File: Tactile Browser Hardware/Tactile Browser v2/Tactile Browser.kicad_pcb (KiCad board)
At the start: 4 copper layers, 74.2 x 113.2 mm, 132 parts, among them SW1 SW_Push, SW10 SW_Push, SW11 SW_Push, SW12 SW_Push, SW13 SW_Push, SW14 SW_Push, SW15 SW_Push, SW16 SW_Push, SW17 SW_Push, SW18 SW_Push, SW2 SW_Push, SW3 SW_Push, SW4 SW_Push, SW5 SW_Push, SW6 SW_Push, SW7 SW_Push, SW8 SW_Push, SW9 SW_Push

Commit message: PCB almost done!
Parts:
- removed 100uF1, 100uF2: C, Capacitor_SMD:C_0805_2012Metric
- uF10: renamed from 100uF10; moved to B.Cu
- uF9: renamed from 100uF9; moved to B.Cu
- moved uF8 127.6 mm to (51.0, 110.8), turned to 90 degrees
- moved uF18 113.8 mm to (87.0, 129.0), turned to 90 degrees
- moved uF17 112.7 mm to (87.0, 124.7), turned to 90 degrees
- moved uF7 107.6 mm to (56.8, 110.8), turned to -90 degrees
- moved uF15 100.8 mm to (88.2, 105.0), turned to 90 degrees
- moved uF6 96.7 mm to (50.2, 75.8), turned to 90 degrees
- moved uF4 95.4 mm to (50.5, 66.8), turned to 90 degrees
- moved uF16 92.6 mm to (88.2, 97.5), turned to -90 degrees
- moved uF5 91.5 mm to (57.2, 75.8), turned to -90 degrees
- moved 5V 83.3 mm to (64.0, 120.7), turned to -90 degrees
- moved uF3 77.2 mm to (56.8, 66.5), turned to 90 degrees
- moved uF13 65.0 mm to (90.8, 76.2), turned to 90 degrees
- moved uF11 63.0 mm to (91.0, 67.0), turned to -90 degrees
- moved uF9 57.5 mm to (88.5, 41.0), turned to -90 degrees
- moved uF14 57.0 mm to (98.2, 76.0), turned to 90 degrees
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- renumbered 100nF1 to uF1, 100uF11 to uF11, 100uF12 to uF12, 100uF13 to uF13, 100uF14 to uF14, 100uF15 to uF15, 100uF16 to uF16, 100uF17 to uF17, 100uF18 to uF18, 100nF2 to uF2, 100uF3 to uF3, 100uF4 to uF4, 100uF5 to uF5, 100uF6 to uF6, 100uF7 to uF7, 100uF8 to uF8
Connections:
- DS10 pad 2: S6_out1 -> S5_out2
- DS11 pad 2: S5_out2 -> S6_out1
- DS12 pad 2: S5_out1 -> S6_out2
- DS9 pad 2: S6_out2 -> S5_out1
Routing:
- net 12V: track 46.8 -> 195.2 mm, vias 4 -> 6
- net Col1: track 9.19 -> 122.4 mm, vias 0 -> 2
- net Row1: track 22.3 -> 130.5 mm, vias 0 -> 1
- net Row2: track 1.54 -> 108.7 mm, vias 0 -> 1
- net Col2: track 0.00 -> 104.1 mm, vias 0 -> 5
- net Col3: track 0.00 -> 100.7 mm
- net Row3: track 0.00 -> 99.4 mm, vias 0 -> 3
- net Row5: track 0.00 -> 93.7 mm, vias 0 -> 5
- net Row4: track 0.00 -> 92.0 mm, vias 0 -> 1
- net DATA: track 0.00 -> 91.6 mm, vias 0 -> 1
- net Row6: track 0.00 -> 81.5 mm, vias 0 -> 3
- net CLOCK: track 0.00 -> 49.6 mm, vias 0 -> 2
- net LATCH: track 0.00 -> 47.2 mm, vias 0 -> 2
- net GND: track 22.1 -> 67.2 mm
- net 5V: track 13.5 -> 40.5 mm, vias 2 -> 7
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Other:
- board size 74.2 x 113.2 mm -> 74.5 x 110.2 mm

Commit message: more pcb work
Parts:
- turned DS18 to -90 degrees
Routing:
- net STBY: track 27.5 -> 112.2 mm, vias 2 -> 5
- net CLOCK: track 49.6 -> 106.7 mm, vias 2 -> 5
- net LATCH: track 47.2 -> 102.9 mm, vias 2 -> 3
- net PWM: track 23.0 -> 75.0 mm, vias 2 -> 5
- net GND: track 67.2 -> 109.3 mm, vias 2 -> 15
- net Overflow1: track 0.00 -> 41.9 mm, vias 0 -> 2
- net 12V: track 195.2 -> 231.6 mm, vias 6 -> 15
- net 5V: track 40.5 -> 56.3 mm
- net S9_out1: track 0.00 -> 15.4 mm, vias 0 -> 1
- net S9_out2: track 0.00 -> 14.6 mm
- net (no net): track 4.91 -> 0.00 mm
- net S5_in1: track 8.54 -> 9.68 mm

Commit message: almost done with pcb!
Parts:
- moved uF11 7.00 mm to (98.0, 67.0)
- moved uF12 6.75 mm to (91.0, 67.0)
- moved uF9 4.00 mm to (88.5, 37.0), turned to 90 degrees
- moved uF10 3.80 mm to (88.5, 40.8), turned to 90 degrees
- moved uF17 0.85 mm to (87.8, 124.3)
- moved uF18 0.85 mm to (87.8, 128.6)
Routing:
- net PWM: track 75.0 -> 369.4 mm, vias 5 -> 16
- net 12V: track 231.6 -> 410.2 mm, vias 15 -> 67
- net GND: track 109.3 -> 257.5 mm, vias 15 -> 57
- net STBY: track 112.2 -> 214.1 mm, vias 5 -> 12
- net 5V: track 56.3 -> 148.4 mm, vias 7 -> 16
- net Overflow2: track 0.00 -> 85.5 mm, vias 0 -> 2
- net SDA: track 0.00 -> 62.6 mm
- net Overflow3: track 0.00 -> 60.0 mm, vias 0 -> 2
- net SCL: track 0.00 -> 53.3 mm
- net S10_out1: track 0.00 -> 46.8 mm
- net S12_out1: track 0.00 -> 43.8 mm
- net S18_out1: track 0.00 -> 41.2 mm
- net S16_out1: track 0.00 -> 39.3 mm
- net S14_out2: track 0.00 -> 37.0 mm, vias 0 -> 1
- net S18_out2: track 0.00 -> 36.4 mm, vias 0 -> 1
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
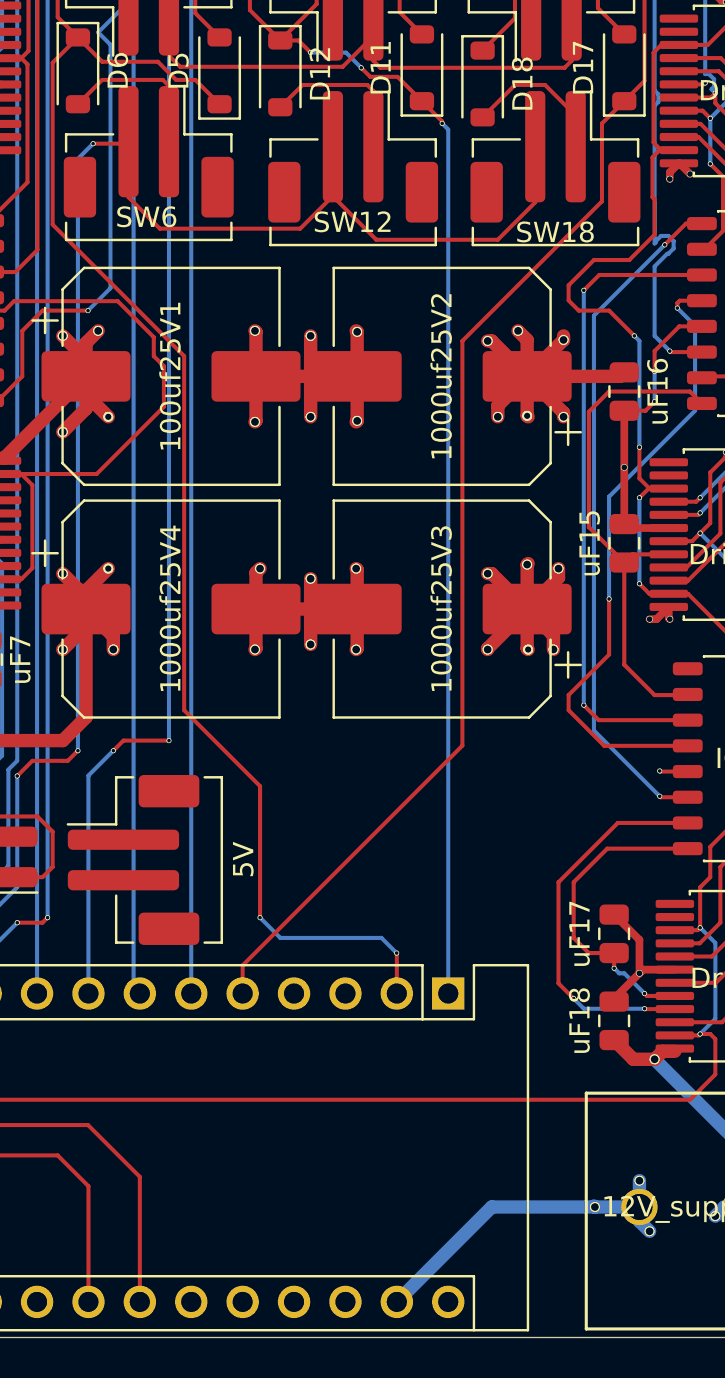
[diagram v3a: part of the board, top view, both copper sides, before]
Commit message: ground +12V planes
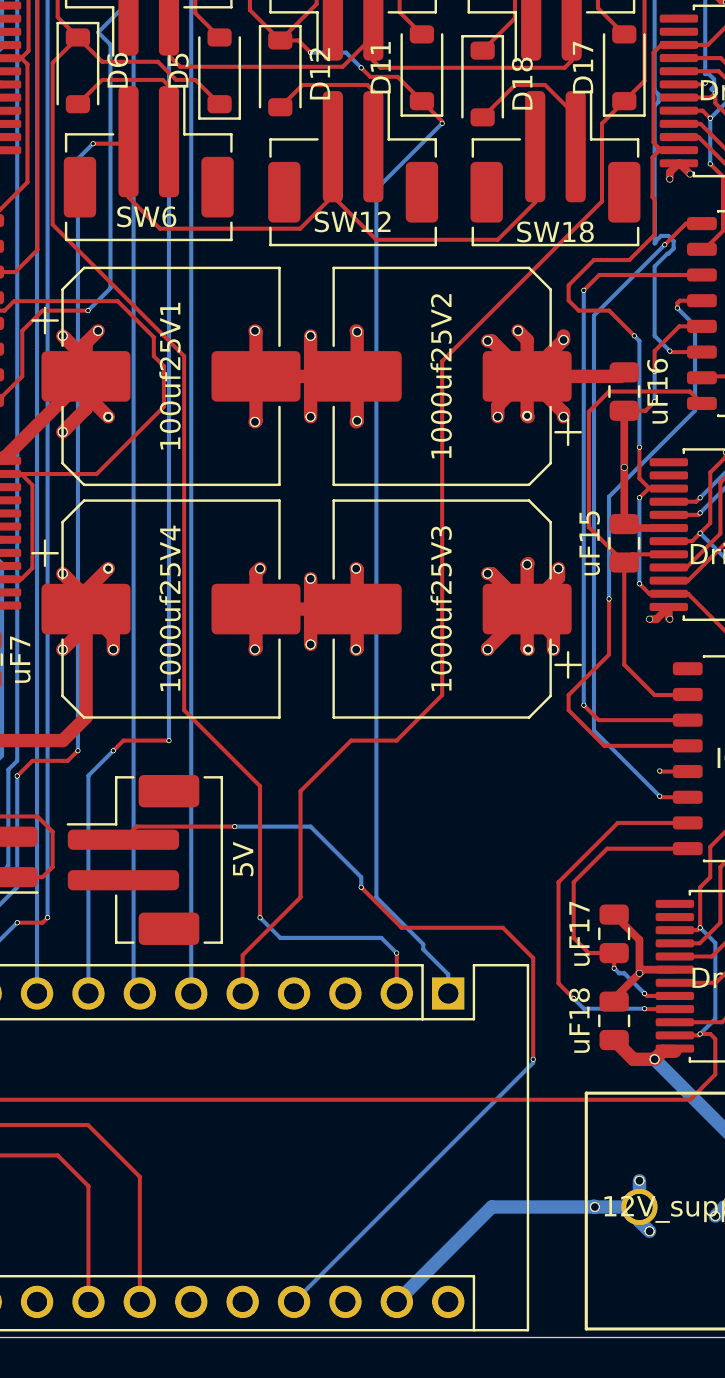
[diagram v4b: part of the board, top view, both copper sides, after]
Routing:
- net 5V: track 148.4 -> 193.8 mm, vias 16 -> 19
- net Col2: track 104.1 -> 106.8 mm
- net Col3: track 100.7 -> 102.0 mm
- removed copper zone on In2.Cu, net 12V
- removed copper zone on In1.Cu, net GND
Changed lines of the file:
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@@
 		(net 8)
 	)
+	(gr_poly
+		(pts
+			(xy 37 34) (xy 111.5 34) (xy 111.5 144.25) (xy 37 144.25)
+		)
+		(stroke
+			(width 0.2)
+			(type solid)
+		)
+		(fill yes)
+		(layer "In1.Cu")
+	)
 	(gr_rect
 		(start 37 34)
@@
 	)
 	(segment
+		(start 82.25 124)
+		(end 83.75 125.5)
+		(width 0.2032)
+		(layer "F.Cu")
+		(net 1)
+	)
+	(segment
 		(start 56.8625 89.055)
 		(end 58.7558 87.1617)
@@
 	)
 	(segment
+		(start 77.25 124)
+		(end 82.25 124)
+		(width 0.2032)
+		(layer "F.Cu")
+		(net 1)
+	)
+	(segment
 		(start 91.497401 97.5)
 		(end 87.5 97.5)
@@
 	)
 	(segment
+		(start 83.75 125.5)
+		(end 83.75 130.5)
+		(width 0.2032)
+		(layer "F.Cu")
+		(net 1)
+	)
+	(segment
 		(start 90.950001 61.6951)
 		(end 92.3049 61.6951)
@@
 	)
 	(segment
+		(start 64.15 119)
+		(end 69 119)
+		(width 0.2032)
+		(layer "F.Cu")
+		(net 1)
+	)
+	(segment
 		(start 89.25 38.870098)
 		(end 89.25 38.75)
@@
 	)
 	(segment
+		(start 63.5 119.65)
+		(end 64.15 119)
+		(width 0.2032)
+		(layer "F.Cu")
+		(net 1)
+	)
+	(segment
 		(start 91.95 77.2)
 		(end 90.75 77.2)
@@
 	)
 	(segment
+		(start 75.25 122)
+		(end 77.25 124)
+		(width 0.2032)
+		(layer "F.Cu")
+		(net 1)
+	)
+	(segment
 		(start 98 66.05)
 		(end 96.8 66.05)
@@
 	)
 	(via
+		(at 69 119)
+		(size 0.254)
+		(drill 0.1778)
+		(layers "F.Cu" "B.Cu")
+		(net 1)
+	)
+	(via
 		(at 92.5 86.25)
 		(size 0.254)
@@
 	)
 	(via
+		(at 83.75 130.5)
+		(size 0.254)
+		(drill 0.1778)
+		(layers "F.Cu" "B.Cu")
+		(net 1)
+	)
+	(via
 		(at 55.75 96.75)
 		(size 0.254)
@@
 	)
 	(via
+		(at 75.25 122)
+		(size 0.254)
+		(drill 0.1778)
+		(layers "F.Cu" "B.Cu")
+		(net 1)
+	)
+	(via
 		(at 90.5 44.75)
 		(size 0.254)
@@
 	)
 	(segment
+		(start 83.75 130.67)
+		(end 71.93 142.49)
+		(width 0.2032)
+		(layer "B.Cu")
+		(net 1)
+	)
+	(segment
 		(start 55.5 43.75)
 		(end 55.75 44)
@@
 	)
 	(segment
+		(start 75.25 122)
+		(end 75.25 121.5)
+		(width 0.2032)
+		(layer "B.Cu")
+		(net 1)
+	)
+	(segment
 		(start 93.5 83)
 		(end 93.5 78.5)
@@
 	)
 	(segment
+		(start 83.75 130.5)
+		(end 83.75 130.67)
+		(width 0.2032)
+		(layer "B.Cu")
+		(net 1)
+	)
+	(segment
 		(start 92.5 84)
 		(end 92.5 86.25)
@@
 	)
 	(segment
+		(start 75.25 121.5)
+		(end 72.75 119)
+		(width 0.2032)
+		(layer "B.Cu")
+		(net 1)
+	)
+	(segment
 		(start 59.25 38)
 		(end 58.75 37.5)
@@
 	)
 	(segment
+		(start 72.75 119)
+		(end 69 119)
+		(width 0.2032)
+		(layer "B.Cu")
+		(net 1)
+	)
+	(segment
 		(start 90.5 44.75)
 		(end 90.75 44.5)
@@
 	)
 	(segment
-		(start 87.149 84.251)
-		(end 87.149 88.101)
-		(width 0.2)
-		(layer "F.Cu")
-		(net 24)
-	)
-	(segment
 		(start 87.049 64.599)
 		(end 88.25 65.8)
@@
 	)
 	(segment
-		(start 81.25 44.5)
-		(end 82.451 45.701)
+		(start 69.39 127.25)
+		(end 69.39 125.36)
 		(width 0.2)
 		(layer "F.Cu")
@@
 	)
 	(segment
-		(start 80.25 115)
-		(end 69.39 125.86)
+		(start 72.25 117.25)
+		(end 74.75 114.75)
 		(width 0.2)
 		(layer "F.Cu")
@@
 	)
 	(segment
-		(start 82.849 75.66484)
-		(end 85.01384 73.5)
+		(start 81.25 44.5)
+		(end 82.451 45.701)
 		(width 0.2)
 		(layer "F.Cu")
@@
 	)
 	(segment
-		(start 87.301 45.701)
-		(end 88.25 46.65)
+		(start 82.849 75.66484)
+		(end 85.01384 73.5)
 		(width 0.2)
 		(layer "F.Cu")
@@
 	)
 	(segment
-		(start 88.25 83.15)
-		(end 87.149 84.251)
+		(start 87.301 45.701)
+		(end 88.25 46.65)
 		(width 0.2)
 		(layer "F.Cu")
@@
 	)
 	(segment
-		(start 89.251 74)
-		(end 89.251 66.801)
+		(start 87.149 88.101)
+		(end 79.25 96)
 		(width 0.2)
 		(layer "F.Cu")
@@
 	)
 	(segment
-		(start 69.39 125.86)
-		(end 69.39 127.25)
+		(start 77 114.75)
+		(end 79.25 112.5)
+		(width 0.2)
+		(layer "F.Cu")
+		(net 24)
+	)
+	(segment
+		(start 89.251 74)
+		(end 89.251 66.801)
 		(width 0.2)
 		(layer "F.Cu")
@@
 	)
 	(segment
+		(start 74.75 114.75)
+		(end 77 114.75)
+		(width 0.2)
+		(layer "F.Cu")
+		(net 24)
+	)
+	(segment
+		(start 87.149 84.251)
+		(end 87.149 88.101)
+		(width 0.2)
+		(layer "F.Cu")
+		(net 24)
+	)
+	(segment
+		(start 79.25 96)
+		(end 79.25 112.5)
+		(width 0.2)
+		(layer "F.Cu")
+		(net 24)
+	)
+	(segment
+		(start 69.39 125.36)
+		(end 72.25 122.5)
+		(width 0.2)
+		(layer "F.Cu")
+		(net 24)
+	)
+	(segment
 		(start 82.451 45.701)
 		(end 87.301 45.701)
@@
 	)
 	(segment
-		(start 87.149 88.101)
-		(end 80.25 95)
+		(start 88.25 83.15)
+		(end 87.149 84.251)
 		(width 0.2)
 		(layer "F.Cu")
@@
 	)
 	(segment
-		(start 80.25 95)
-		(end 80.25 115)
+		(start 81.25 62.5)
+		(end 83.349 64.599)
 		(width 0.2)
 		(layer "F.Cu")
@@
 	)
 	(segment
-		(start 81.25 62.5)
-		(end 83.349 64.599)
+		(start 72.25 122.5)
+		(end 72.25 117.25)
 		(width 0.2)
 		(layer "F.Cu")
@@
 	)
 	(segment
-		(start 74.5 80.75)
-		(end 75.25 81.5)
+		(start 79.25 84.25)
+		(end 76 87.5)
+		(width 0.2)
+		(layer "B.Cu")
+		(net 27)
+	)
+	(segment
+		(start 76 122.5)
+		(end 78.317787 124.817787)
 		(width 0.2)
 		(layer "B.Cu")
@@
 	)
 	(segment
-		(start 79.55 127.25)
-		(end 79.55 84.55)
+		(start 78.317787 125.067787)
+		(end 79.55 126.3)
 		(width 0.2)
 		(layer "B.Cu")
@@
 	)
 	(segment
-		(start 79.55 84.55)
-		(end 79.25 84.25)
+		(start 79.55 126.3)
+		(end 79.55 127.25)
+		(width 0.2)
+		(layer "B.Cu")
+		(net 27)
+	)
+	(segment
+		(start 76 87.5)
+		(end 76 122.5)
+		(width 0.2)
+		(layer "B.Cu")
+		(net 27)
+	)
+	(segment
+		(start 78.317787 124.817787)
+		(end 78.317787 125.067787)
+		(width 0.2)
+		(layer "B.Cu")
+		(net 27)
+	)
+	(segment
+		(start 74.5 80.75)
+		(end 75.25 81.5)
 		(width 0.2)
 		(layer "B.Cu")
@@
 		(net 125)
 	)
-	(zone
-		(net 2)
-		(net_name "GND")
-		(layer "In1.Cu")
-		(hatch edge 0.5)
-		(connect_pads
-			(clearance 0.5)
-		)
-		(min_thickness 0.25)
-		(filled_areas_thickness no)
-		(fill yes
-			(thermal_gap 0.5)
-			(thermal_bridge_width 0.5)
-		)
-		(polygon
-			(pts
-				(xy 37 34) (xy 129 34) (xy 129 149) (xy 37 149)
-			)
-		)
-	)
-	(zone
-		(net 3)
-		(net_name "12V")
-		(layer "In2.Cu")
-		(hatch edge 0.5)
-		(priority 1)
-		(connect_pads
-			(clearance 0.5)
-		)
-		(min_thickness 0.25)
-		(filled_areas_thickness no)
-		(fill yes
-			(thermal_gap 0.5)
-			(thermal_bridge_width 0.5)
-		)
-		(polygon
-			(pts
-				(xy 37 34) (xy 129 34) (xy 129 149) (xy 37 149)
-			)
-		)
-	)
 	(embedded_fonts no)

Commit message: DRC
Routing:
- net LATCH: track 133.9 -> 263.1 mm, vias 5 -> 8
- net 5V: track 193.8 -> 299.5 mm, vias 19 -> 23
- net CLOCK: track 140.1 -> 189.3 mm, vias 7 -> 8
- net STBY: track 214.1 -> 257.9 mm, vias 12 -> 13
- net Col3: track 102.0 -> 122.6 mm, vias 0 -> 2
- net Col2: track 106.8 -> 126.1 mm, vias 5 -> 7
- net S17_out1: track 14.9 -> 18.3 mm
- net 12V: track 410.2 -> 412.3 mm, vias 67 -> 69
- net S4_in2: track 13.7 -> 14.7 mm
- net Overflow3: track 60.0 -> 59.0 mm
- net S4_in1: track 14.5 -> 15.5 mm
- net S12_in1: track 17.6 -> 18.4 mm
- net GND: track 257.5 -> 256.8 mm, vias 57 -> 58
- net PWM: track 369.4 -> 368.8 mm, vias 16 -> 17
- net S5_in1: track 9.68 -> 10.2 mm
- added copper zone on In2.Cu, net 12V
- added copper zone on In1.Cu, net GND

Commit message: ran drc, finished routing
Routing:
- net CLOCK: track 189.3 -> 259.9 mm, vias 8 -> 9
- net 5V: track 299.5 -> 335.8 mm, vias 23 -> 24
- net S17_out2: track 15.8 -> 19.4 mm
- net S15_out2: track 13.6 -> 17.1 mm
- net S15_out1: track 15.2 -> 18.6 mm
- net GND: track 256.8 -> 259.2 mm, vias 58 -> 60
- net PWM: track 368.8 -> 369.6 mm

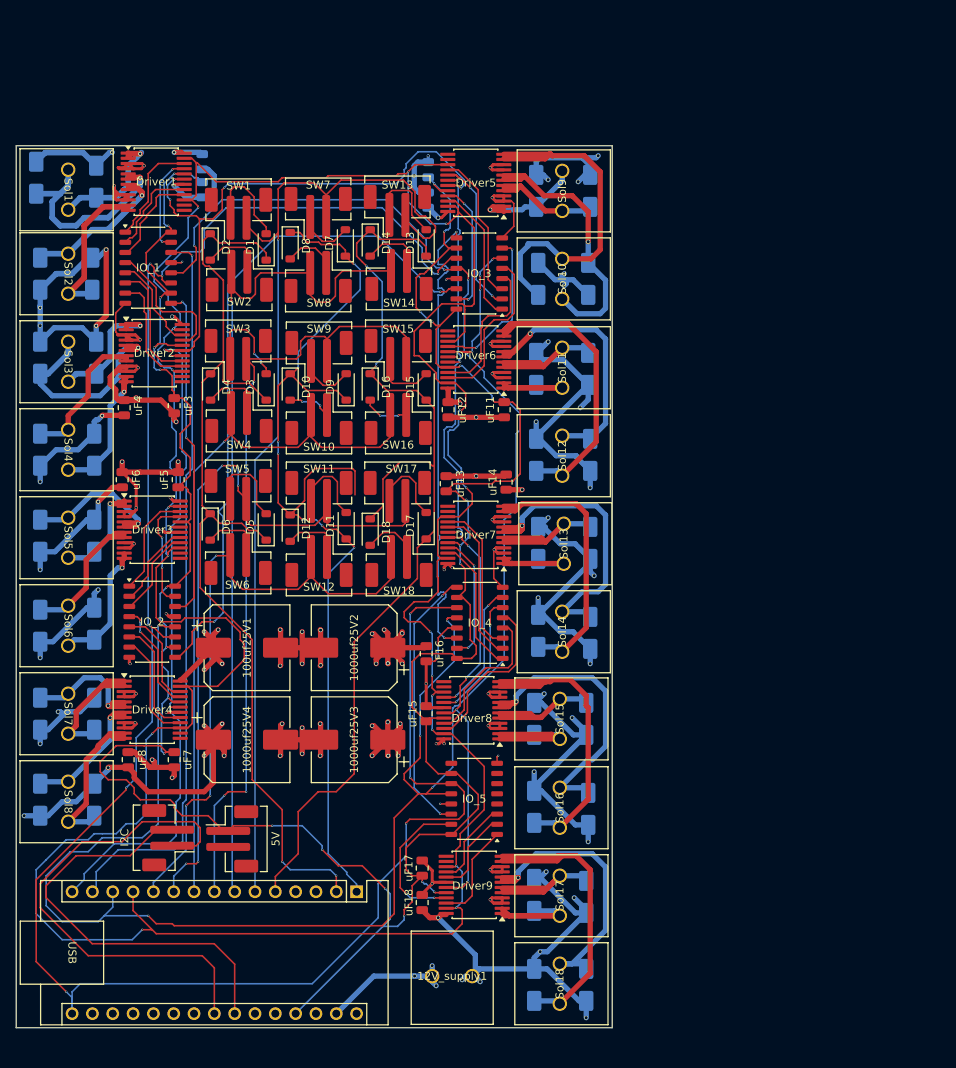
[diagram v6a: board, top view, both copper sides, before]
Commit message: FINISHED PCB
resolved DRC, added drill holes,
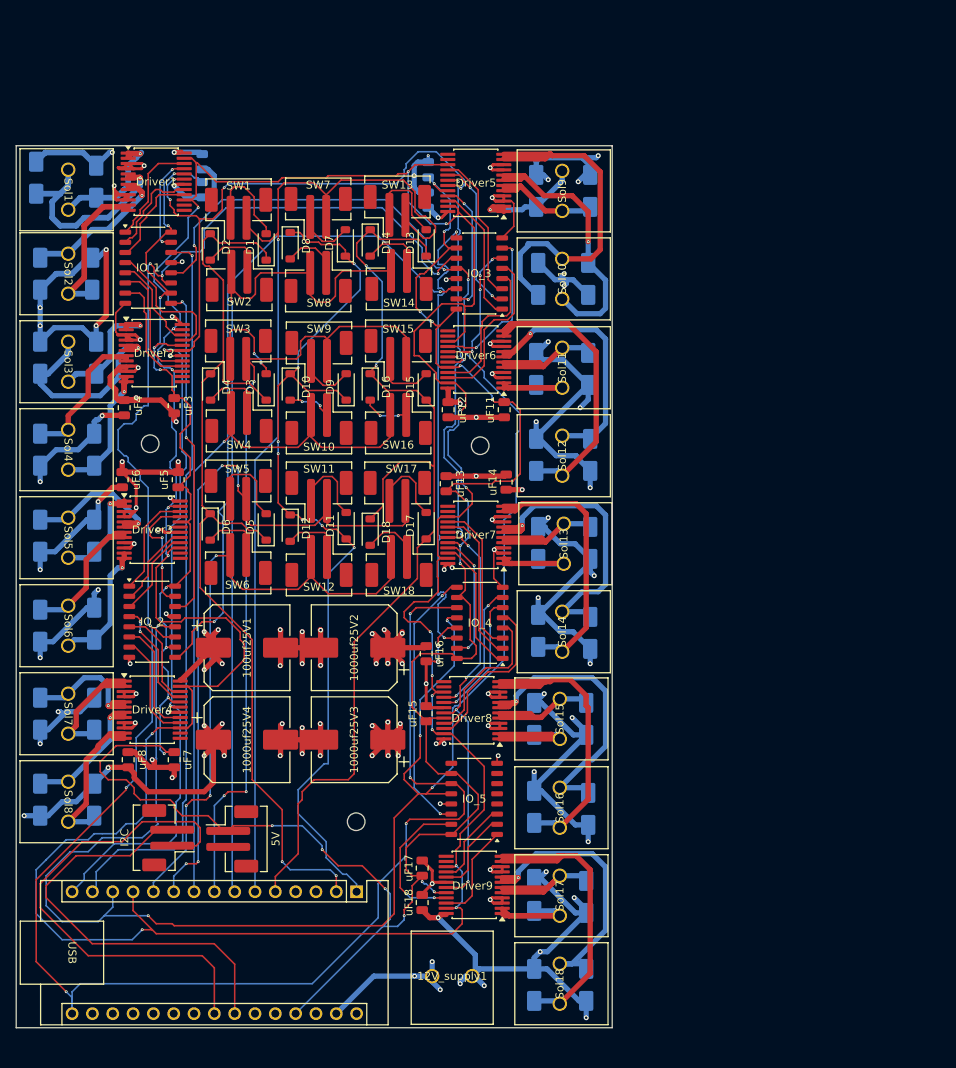
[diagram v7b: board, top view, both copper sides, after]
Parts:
- added REF**: MountingHole_2.2mm_M2, MountingHole:MountingHole_2.2mm_M2, F.Cu at (95.0, 71.5)
- added REF**: MountingHole_2.2mm_M2, MountingHole:MountingHole_2.2mm_M2, F.Cu at (79.5, 118.5)
- added REF**: MountingHole_2.2mm_M2, MountingHole:MountingHole_2.2mm_M2, F.Cu at (53.8, 71.2)
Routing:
- net Col2: track 126.1 -> 114.6 mm
- net CLOCK: track 259.9 -> 264.1 mm
- net S5_in1: track 10.2 -> 11.8 mm
- net STBY: track 257.9 -> 259.2 mm
- net 12V: track 412.3 -> 413.6 mm
- net GND: track 259.2 -> 260.5 mm
- net Col3: track 122.6 -> 123.8 mm
